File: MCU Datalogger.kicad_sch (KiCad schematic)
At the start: 26 parts, among them U1 24LC1025, U2 24LC1025, U3 DS1337S_, U4 ATMEGA328P-AU, Y1 Crystal, Y2 Crystal

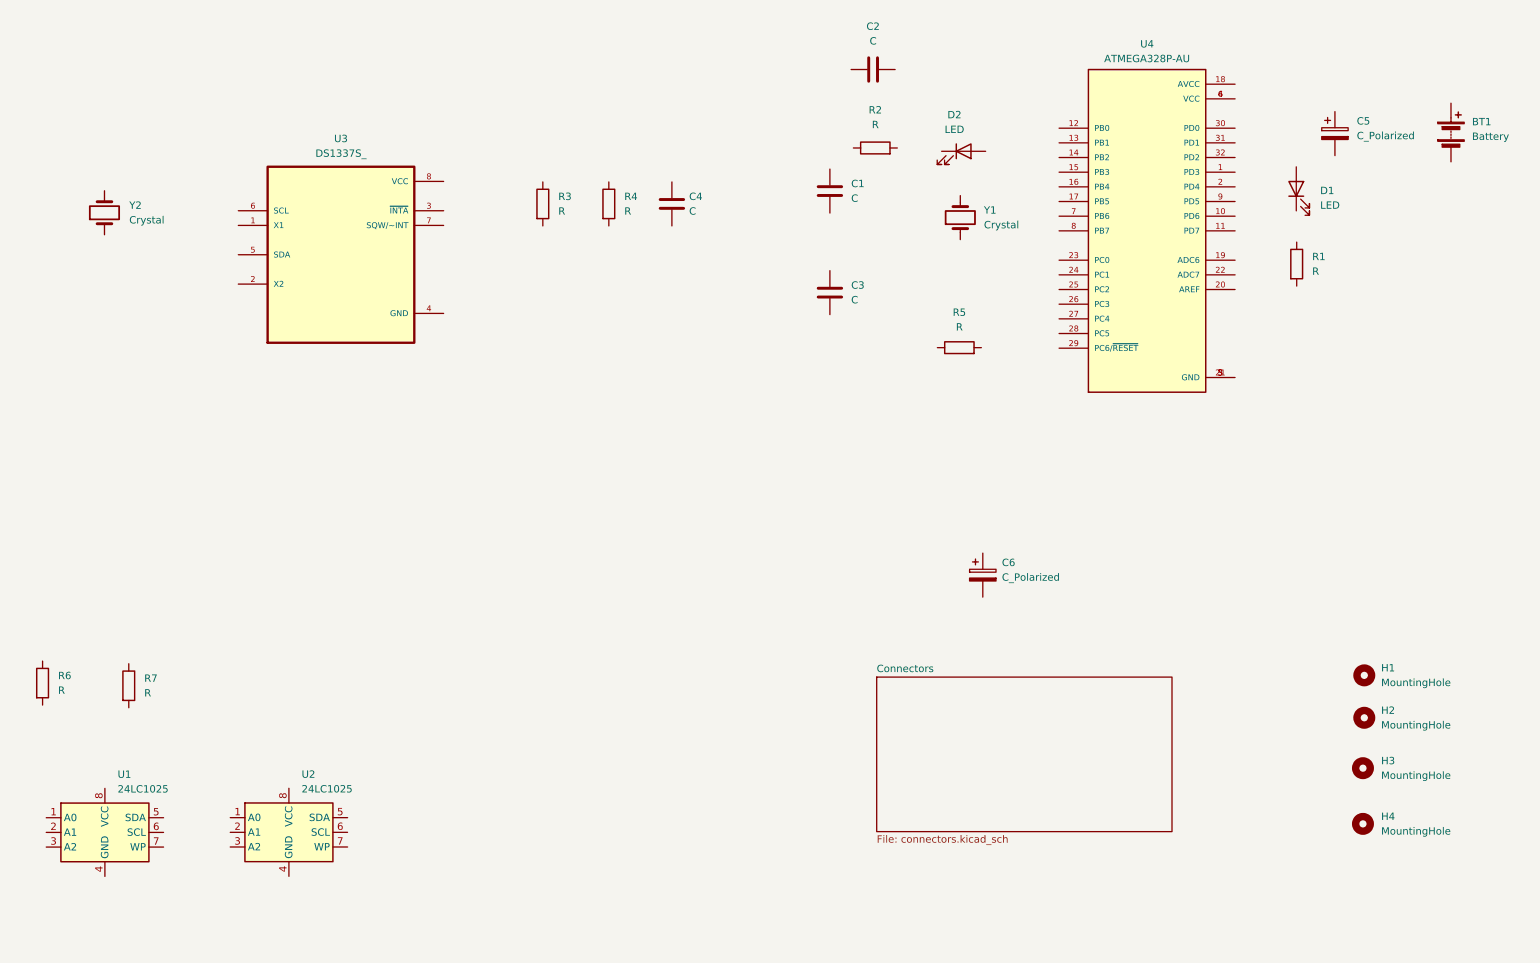
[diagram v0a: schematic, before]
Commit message: Added component values
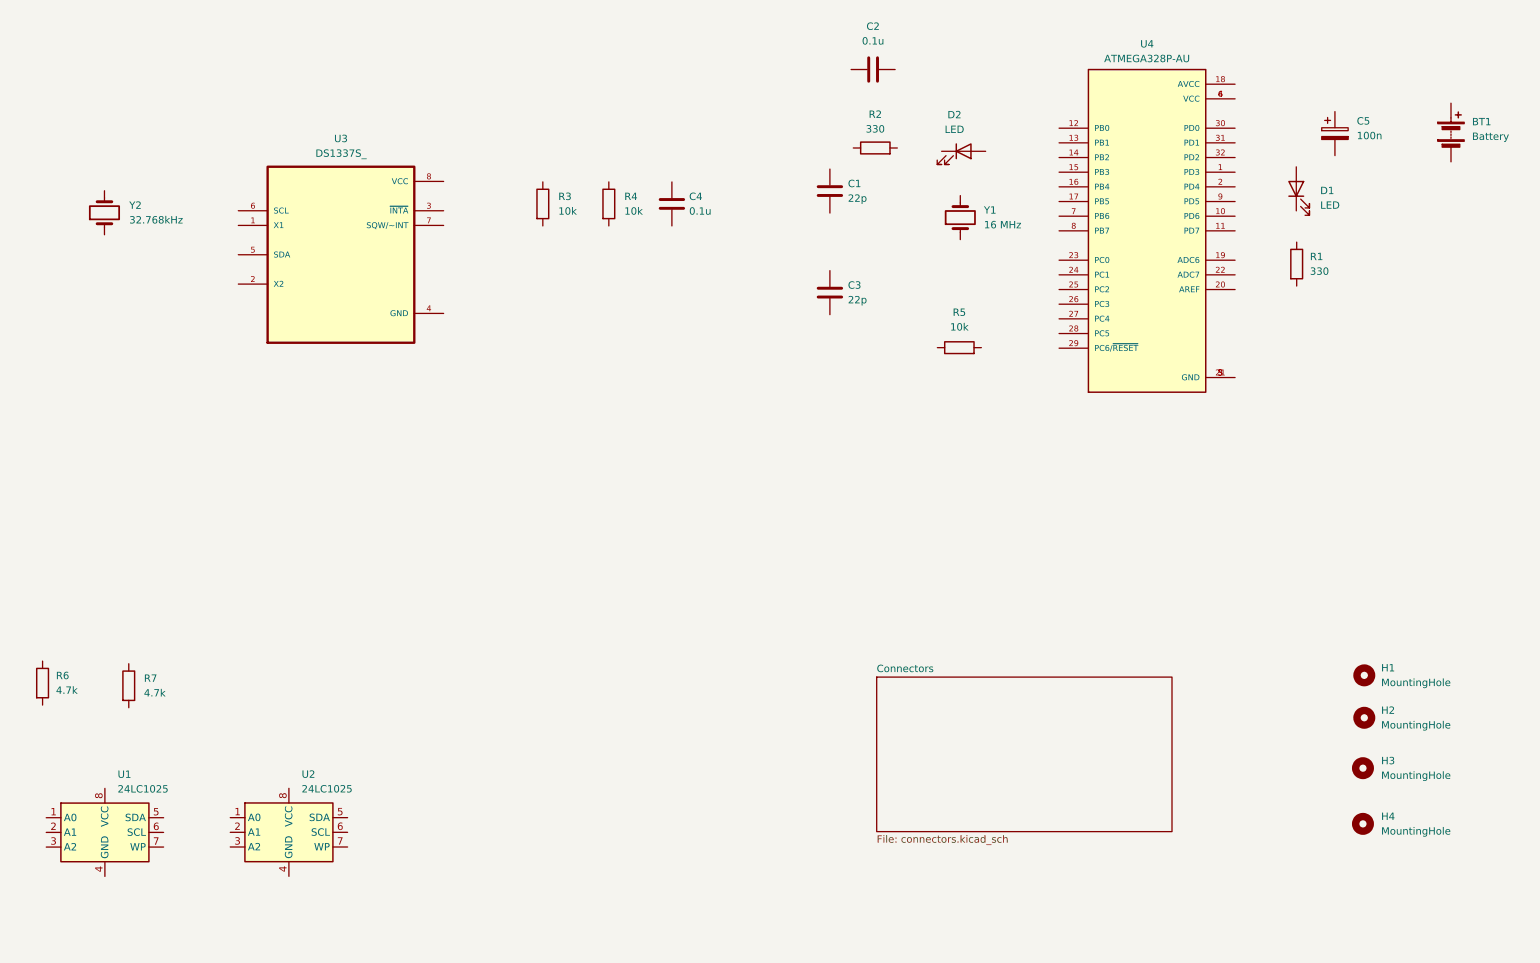
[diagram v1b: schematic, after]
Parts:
- removed C6: C_Polarized, symbol Device:C_Polarized
- C1, C3: value C -> 22p
- C2, C4: value C -> 0.1u
- C5: value C_Polarized -> 100n
- R1, R2: value R -> 330
- R3, R4, R5: value R -> 10k
- R6, R7: value R -> 4.7k
- Y1: value Crystal -> 16 MHz
- Y2: value Crystal -> 32.768kHz
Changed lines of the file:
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@@
   (symbol (lib_id "Device:R") (at 40.5604 134.4944 0) (unit 1)
     (in_bom yes) (on_board yes) (dnp no) (fields_autoplaced)
-    (property "Reference" "R7" (at 43.233 133.2244 0)
-      (effects (font (size 1.27 1.27)) (justify left))
-    )
-    (property "Value" "R" (at 43.233 135.7644 0)
+    (property "Reference" "R7" (at 43.18 133.2244 0)
+      (effects (font (size 1.27 1.27)) (justify left))
+    )
+    (property "Value" "4.7k" (at 43.18 135.7644 0)
       (effects (font (size 1.27 1.27)) (justify left))
     )
@@
       (effects (font (size 1.27 1.27)) (justify left))
     )
-    (property "Value" "R" (at 114.9406 52.324 0)
+    (property "Value" "10k" (at 114.9406 52.324 0)
       (effects (font (size 1.27 1.27)) (justify left))
     )
@@
       (effects (font (size 1.27 1.27)) hide)
     )
+    (property "Purpose" "" (at 112.268 51.054 0)
+      (effects (font (size 1.27 1.27)))
+    )
     (pin "2")
     (pin "1")
@@
   (symbol (lib_id "Device:C") (at 161.9849 48.827 0) (unit 1)
     (in_bom yes) (on_board yes) (dnp no) (fields_autoplaced)
-    (property "Reference" "C1" (at 165.6642 47.557 0)
-      (effects (font (size 1.27 1.27)) (justify left))
-    )
-    (property "Value" "C" (at 165.6642 50.097 0)
+    (property "Reference" "C1" (at 165.1 47.557 0)
+      (effects (font (size 1.27 1.27)) (justify left))
+    )
+    (property "Value" "22p" (at 165.1 50.097 0)
       (effects (font (size 1.27 1.27)) (justify left))
     )
@@
       (effects (font (size 1.27 1.27)) (justify left))
     )
-    (property "Value" "C_Polarized" (at 253.2265 39.256 0)
+    (property "Value" "100n" (at 253.2265 39.256 0)
       (effects (font (size 1.27 1.27)) (justify left))
     )
@@
       (effects (font (size 1.27 1.27)) hide)
     )
+    (property "Purpose" "" (at 249.4474 38.875 0)
+      (effects (font (size 1.27 1.27)))
+    )
     (pin "2")
     (pin "1")
@@
   (symbol (lib_id "Device:R") (at 242.824 61.468 0) (unit 1)
     (in_bom yes) (on_board yes) (dnp no) (fields_autoplaced)
-    (property "Reference" "R1" (at 245.4966 60.198 0)
-      (effects (font (size 1.27 1.27)) (justify left))
-    )
-    (property "Value" "R" (at 245.4966 62.738 0)
+    (property "Reference" "R1" (at 245.11 60.198 0)
+      (effects (font (size 1.27 1.27)) (justify left))
+    )
+    (property "Value" "330" (at 245.11 62.738 0)
       (effects (font (size 1.27 1.27)) (justify left))
     )
@@
   (symbol (lib_id "Device:R") (at 169.8493 41.363 90) (unit 1)
     (in_bom yes) (on_board yes) (dnp no) (fields_autoplaced)
-    (property "Reference" "R2" (at 169.8493 34.7991 90)
-      (effects (font (size 1.27 1.27)))
-    )
-    (property "Value" "R" (at 169.8493 37.3391 90)
+    (property "Reference" "R2" (at 169.8493 35.56 90)
+      (effects (font (size 1.27 1.27)))
+    )
+    (property "Value" "330" (at 169.8493 38.1 90)
       (effects (font (size 1.27 1.27)))
     )
@@
       (effects (font (size 1.27 1.27)) (justify left))
     )
-    (property "Value" "R" (at 126.3706 52.324 0)
+    (property "Value" "10k" (at 126.3706 52.324 0)
       (effects (font (size 1.27 1.27)) (justify left))
     )
@@
       (effects (font (size 1.27 1.27)) hide)
     )
+    (property "Purpose" "" (at 123.698 51.054 0)
+      (effects (font (size 1.27 1.27)))
+    )
     (pin "2")
     (pin "1")
@@
   (symbol (lib_id "Device:C") (at 161.9849 66.4166 0) (unit 1)
     (in_bom yes) (on_board yes) (dnp no) (fields_autoplaced)
-    (property "Reference" "C3" (at 165.6642 65.1466 0)
-      (effects (font (size 1.27 1.27)) (justify left))
-    )
-    (property "Value" "C" (at 165.6642 67.6866 0)
+    (property "Reference" "C3" (at 165.1 65.1466 0)
+      (effects (font (size 1.27 1.27)) (justify left))
+    )
+    (property "Value" "22p" (at 165.1 67.6866 0)
       (effects (font (size 1.27 1.27)) (justify left))
     )
@@
     (property "Datasheet" "~" (at 161.9849 66.4166 0)
       (effects (font (size 1.27 1.27)) hide)
+    )
+    (property "Purpose" "" (at 161.9849 66.4166 0)
+      (effects (font (size 1.27 1.27)))
     )
     (pin "2")
@@
       (effects (font (size 1.27 1.27)) (justify right))
     )
-    (property "Value" "C" (at 137.6003 52.324 0)
+    (property "Value" "0.1u" (at 137.6003 52.324 0)
       (effects (font (size 1.27 1.27)) (justify right))
     )
@@
       (effects (font (size 1.27 1.27)) hide)
     )
+    (property "Purpose" "" (at 134.62 51.054 0)
+      (effects (font (size 1.27 1.27)))
+    )
     (pin "2")
     (pin "1")
@@
     )
   )
-  (symbol (lib_id "Device:C_Polarized") (at 188.462 115.3383 0) (unit 1)
-    (in_bom yes) (on_board yes) (dnp no) (fields_autoplaced)
-    (property "Reference" "C6" (at 191.77 113.1793 0)
-      (effects (font (size 1.27 1.27)) (justify left))
-    )
-    (property "Value" "C_Polarized" (at 191.77 115.7193 0)
-      (effects (font (size 1.27 1.27)) (justify left))
-    )
-    (property "Footprint" "" (at 189.4272 119.1483 0)
-      (effects (font (size 1.27 1.27)) hide)
-    )
-    (property "Datasheet" "~" (at 188.462 115.3383 0)
-      (effects (font (size 1.27 1.27)) hide)
-    )
-    (pin "2")
-    (pin "1")
-    (instances
-      (project "MCU Datalogger"
-        (path "/701cd918-e6eb-422f-bf82-18f80ff441f1"
-          (reference "C6") (unit 1)
-        )
-      )
-    )
-  )
   (symbol (lib_id "Device:Battery") (at 269.5428 38.6836 0) (unit 1)
     (in_bom yes) (on_board yes) (dnp no) (fields_autoplaced)
@@
       (effects (font (size 1.27 1.27)))
     )
-    (property "Value" "R" (at 184.404 72.39 90)
+    (property "Value" "10k" (at 184.404 72.39 90)
       (effects (font (size 1.27 1.27)))
     )
@@
       (effects (font (size 1.27 1.27)))
     )
-    (property "Value" "C" (at 169.4666 22.86 90)
+    (property "Value" "0.1u" (at 169.4666 22.86 90)
       (effects (font (size 1.27 1.27)))
     )
@@
       (effects (font (size 1.27 1.27)) hide)
     )
+    (property "Purpose" "" (at 169.4666 27.7747 0)
+      (effects (font (size 1.27 1.27)))
+    )
     (pin "2")
     (pin "1")
@@
   (symbol (lib_id "Device:R") (at 25.6325 134.0351 0) (unit 1)
     (in_bom yes) (on_board yes) (dnp no) (fields_autoplaced)
-    (property "Reference" "R6" (at 28.3051 132.7651 0)
-      (effects (font (size 1.27 1.27)) (justify left))
-    )
-    (property "Value" "R" (at 28.3051 135.3051 0)
+    (property "Reference" "R6" (at 27.94 132.7651 0)
+      (effects (font (size 1.27 1.27)) (justify left))
+    )
+    (property "Value" "4.7k" (at 27.94 135.3051 0)
       (effects (font (size 1.27 1.27)) (justify left))
     )
@@
       (effects (font (size 1.27 1.27)) (justify right))
     )
-    (property "Value" "Crystal" (at 40.64 53.8512 90)
+    (property "Value" "32.768kHz" (at 40.64 53.8512 90)
       (effects (font (size 1.27 1.27)) (justify right))
     )
@@
     (property "Datasheet" "~" (at 36.3518 52.5812 0)
       (effects (font (size 1.27 1.27)) hide)
+    )
+    (property "Purpose" "" (at 36.3518 52.5812 0)
+      (effects (font (size 1.27 1.27)))
     )
     (pin "2")
@@
       (effects (font (size 1.27 1.27)) (justify right))
     )
-    (property "Value" "Crystal" (at 188.6558 54.6902 90)
+    (property "Value" "16 MHz" (at 188.6558 54.6902 90)
       (effects (font (size 1.27 1.27)) (justify right))
     )
@@
       (effects (font (size 1.27 1.27)) hide)
     )
-    (pin "2")
+    (property "Purpose" "" (at 184.5682 53.4202 0)
+      (effects (font (size 1.27 1.27)))
+    )
+    (pin "2")

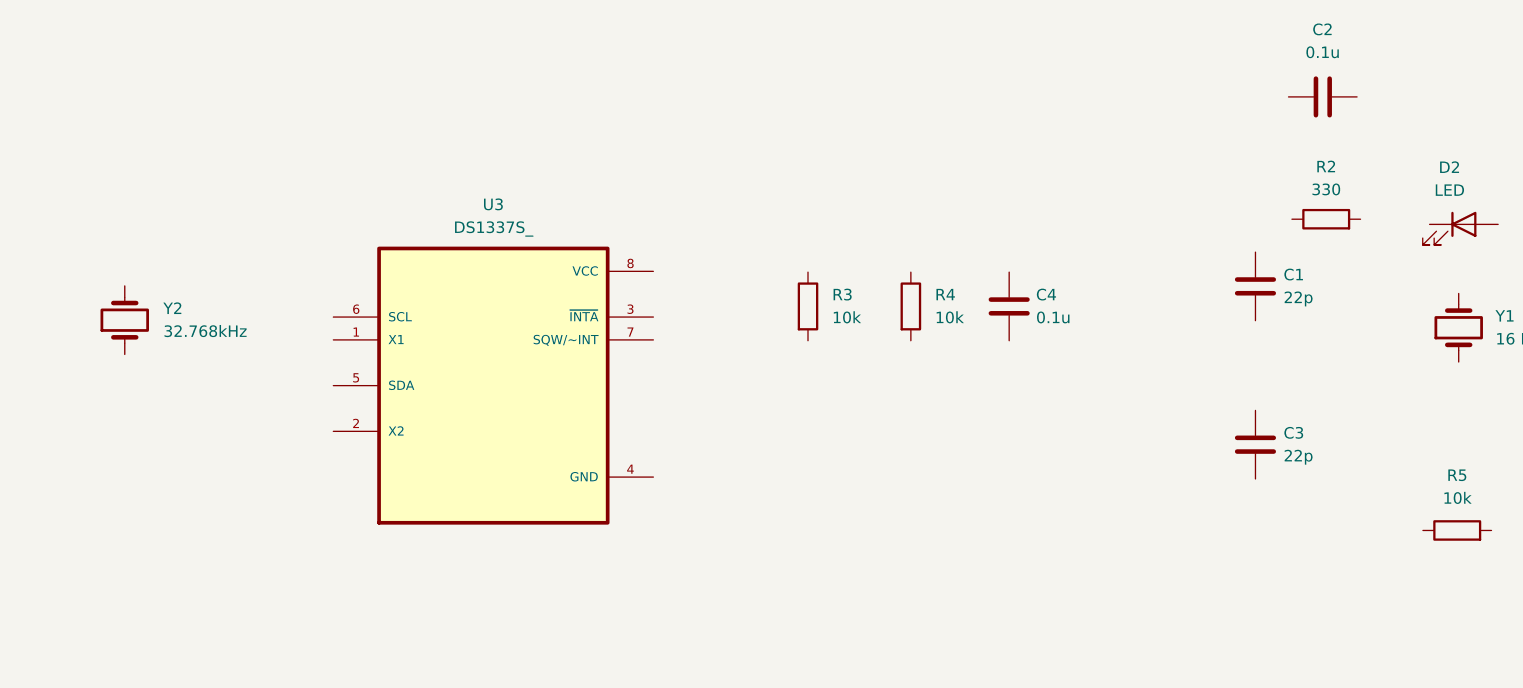
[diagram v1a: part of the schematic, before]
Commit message: completed symbol to footprint assocciations
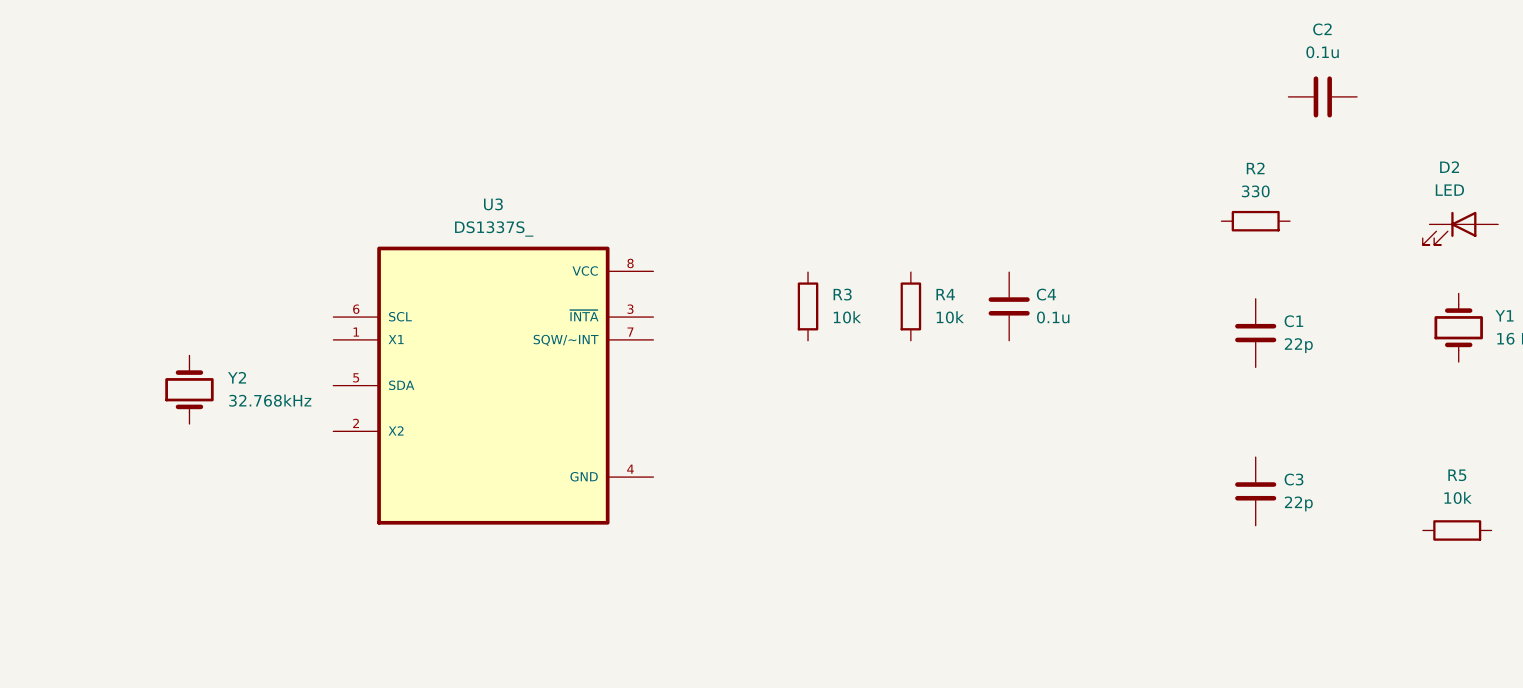
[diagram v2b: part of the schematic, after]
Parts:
- BT1: footprint (none) -> Connector_PinHeader_2.54mm:PinHeader_1x02_P2.54mm_Vertical
- C1, C2, C3, C4, C5: footprint (none) -> Capacitor_SMD:C_0805_2012Metric
- D1, D2: footprint (none) -> LED_SMD:LED_0805_2012Metric
- H1, H2, H3, H4: footprint (none) -> MountingHole:MountingHole_2.1mm
- R1, R2, R3, R4, R5, R6, R7: footprint (none) -> Resistor_SMD:R_0805_2012Metric
- U1, U2: footprint (none) -> Package_SO:SOIC-8_5.23x5.23mm_P1.27mm
- U3: footprint DS1337S_:SOIC127P600X175-8N -> footprints:SOIC127P600X175-8N
- U4: footprint ATMEGA328P-AU:QFP80P900X900X120-32N -> footprints:QFP80P900X900X120-32N
- Y1, Y2: footprint (none) -> Crystal:Crystal_SMD_5032-2Pin_5.0x3.2mm_HandSoldering
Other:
- moved on the sheet: C1, C3, R2, Y2
